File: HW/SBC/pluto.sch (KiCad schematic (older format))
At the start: 0 parts

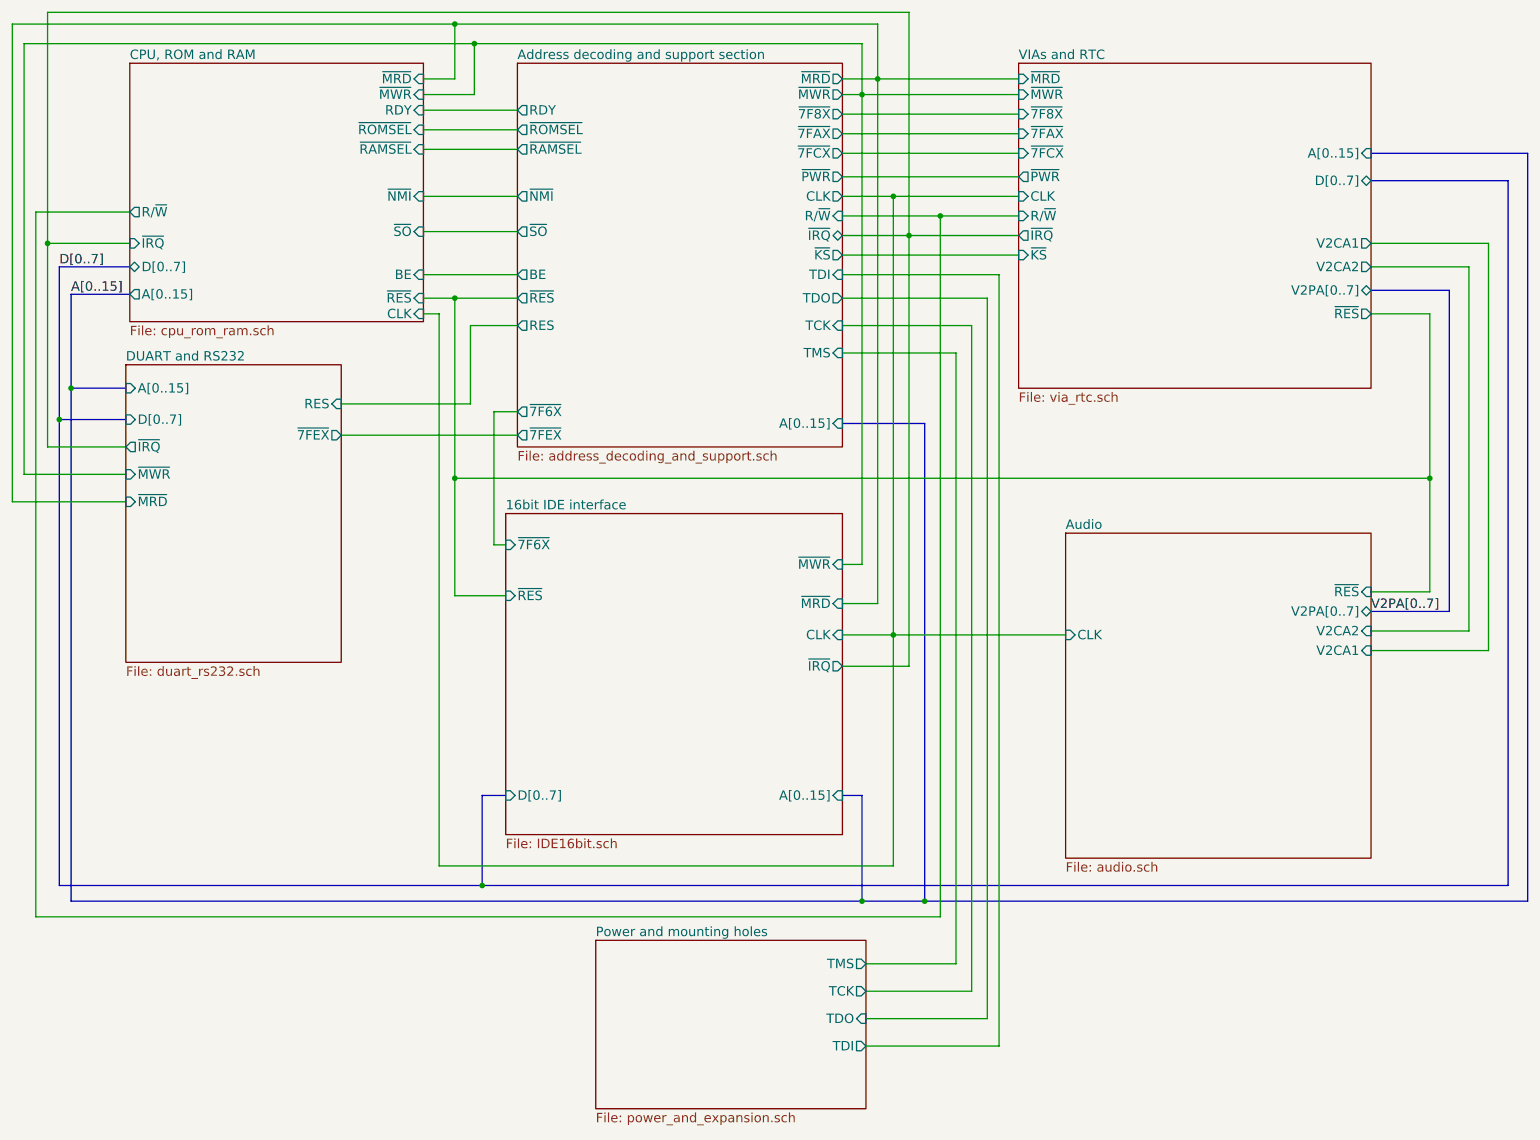
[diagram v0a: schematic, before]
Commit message: Added CPLD to schematics. Updates rest of schematics to use CPLD
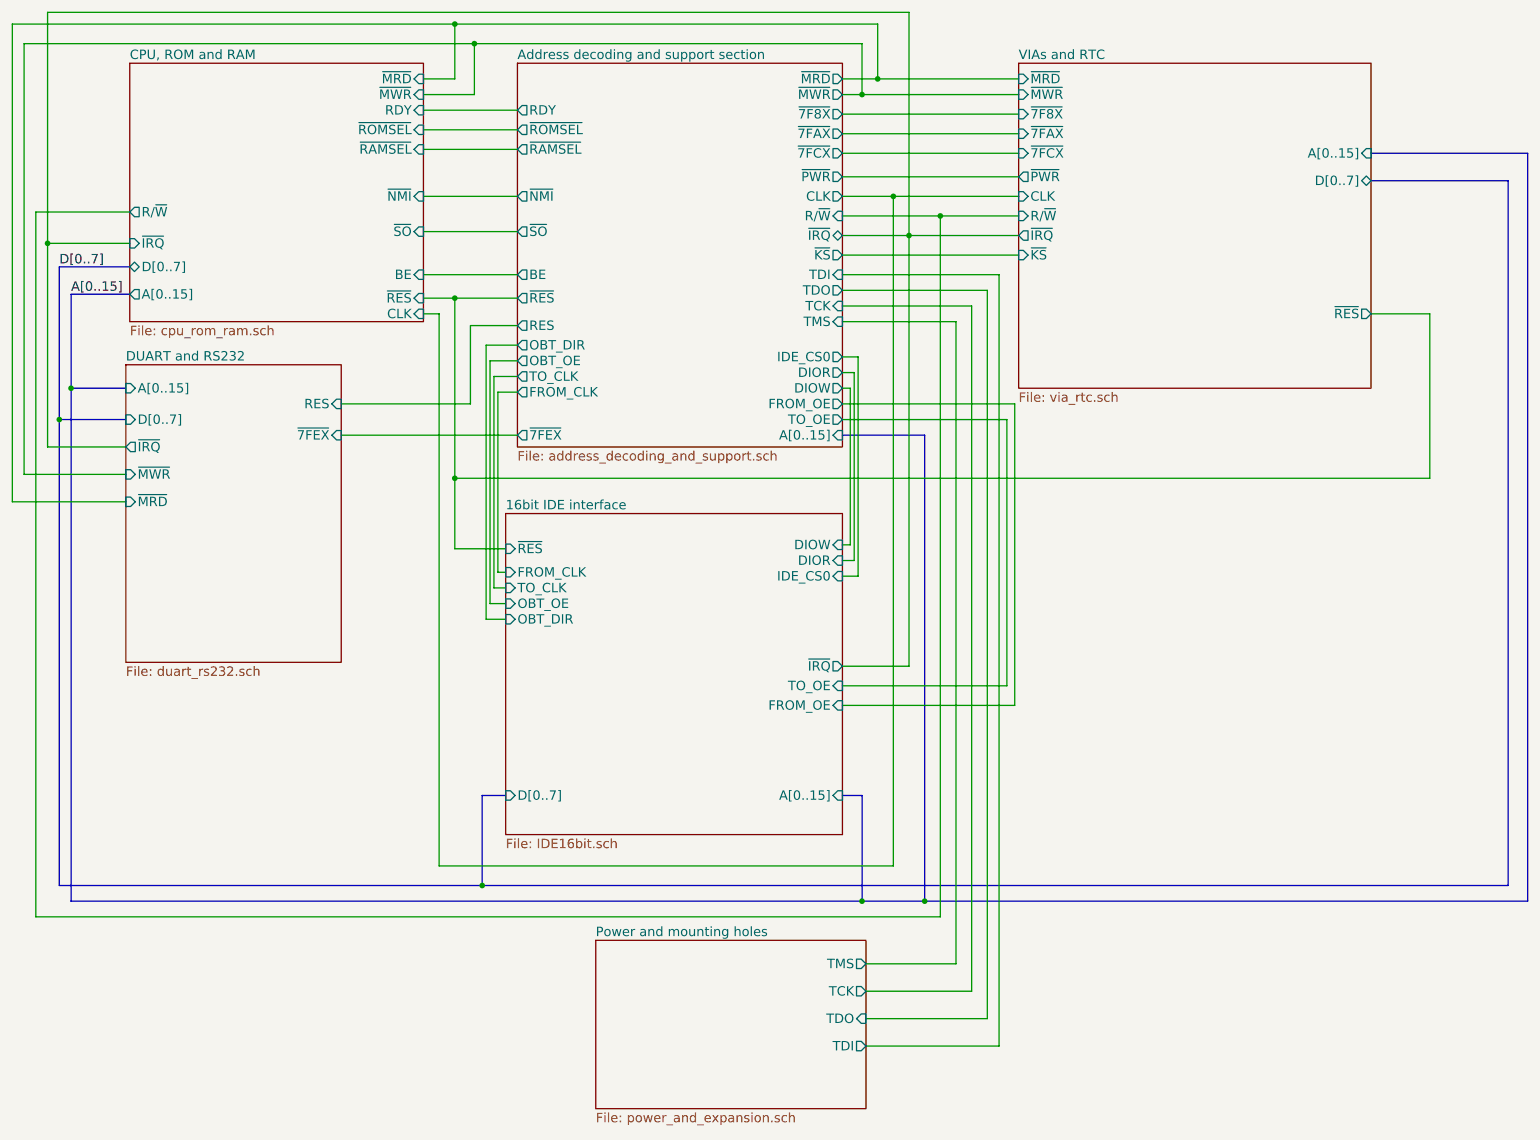
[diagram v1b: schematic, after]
